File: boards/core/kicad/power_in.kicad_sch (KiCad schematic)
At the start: 34 parts, among them J1 USB4085-GF-A, Q1 AO4485, Q2 2N7002, Q3 MMDT3904, U1 CH224Q, U2 USBLC6-2SC6, U3 INA186A1

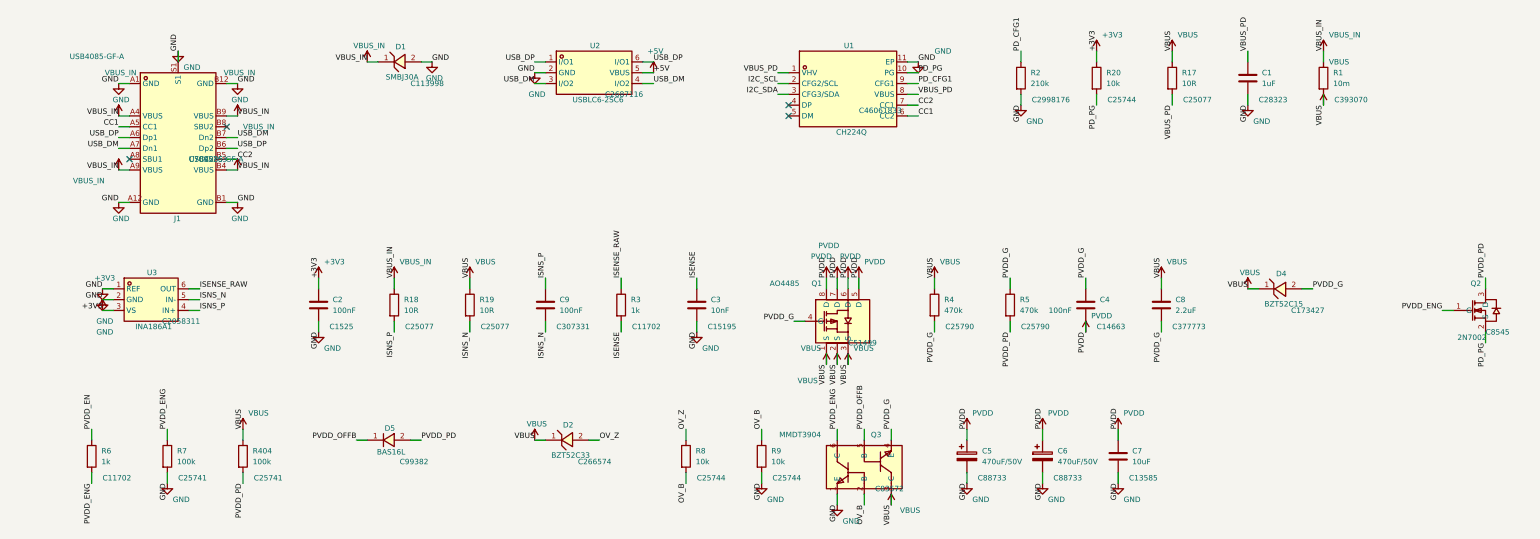
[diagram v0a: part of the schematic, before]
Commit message: core: ESD clamps at the USB-C CC pins and both RCA jacks; speaker and Ethernet lines exempt with reasons (#133)
D6/D9 (NUP2105L) on CC1/CC2, D7/D8 (PESD5V0S2BT) on sub out and line in,
all on B.Cu at their connectors with their own ground vias. KiCad DRC with
schematic parity is clean; check_esd has 0 errors and 4 warnings, judged in
docs/boards/core-esd.md.

Co-Authored-By: Claude Opus 5.5 <noreply@anthropic.com>
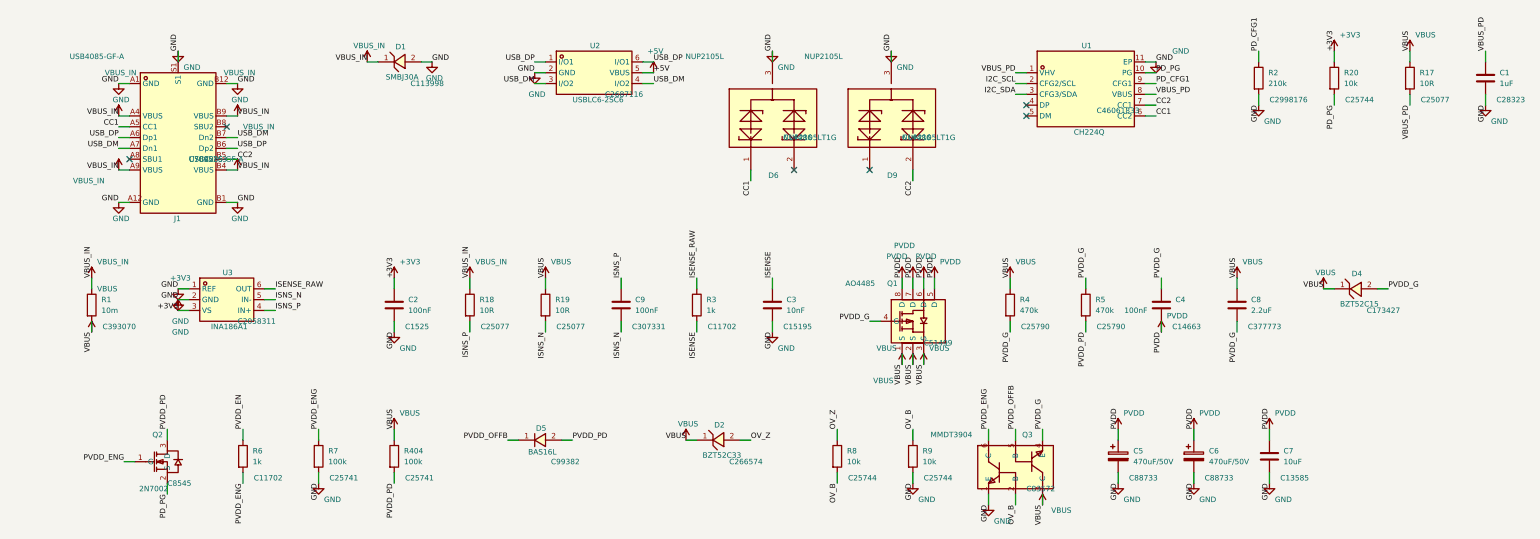
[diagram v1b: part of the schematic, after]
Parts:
- added D6, D9: NUP2105L, aiee:SOT-23-3_L2.9-W1.3-P1.90-LS2.4-BL-2, symbol aiee:NUP2105LT1G
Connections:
- net CC1: now also D6.1
- net CC2: now also D9.2
- net GND: now also D6.3, D9.3
- no-connect marks 4 -> 6
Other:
- moved on the sheet: C1, C2, C3, C4, C5, C6, C7, C8, C9, D2, D4, D5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
